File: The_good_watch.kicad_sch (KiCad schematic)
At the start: 46 parts, among them IC1 DW01A, J1 Main, J2 USB_C_Receptacle_USB2.0, J3 PROG, J4 Screen, J5 Button, J6 Conn_02x07_Counter_Clockwise, M1 Motor_DC, Q1 FS8205A, SW1 SW_Push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

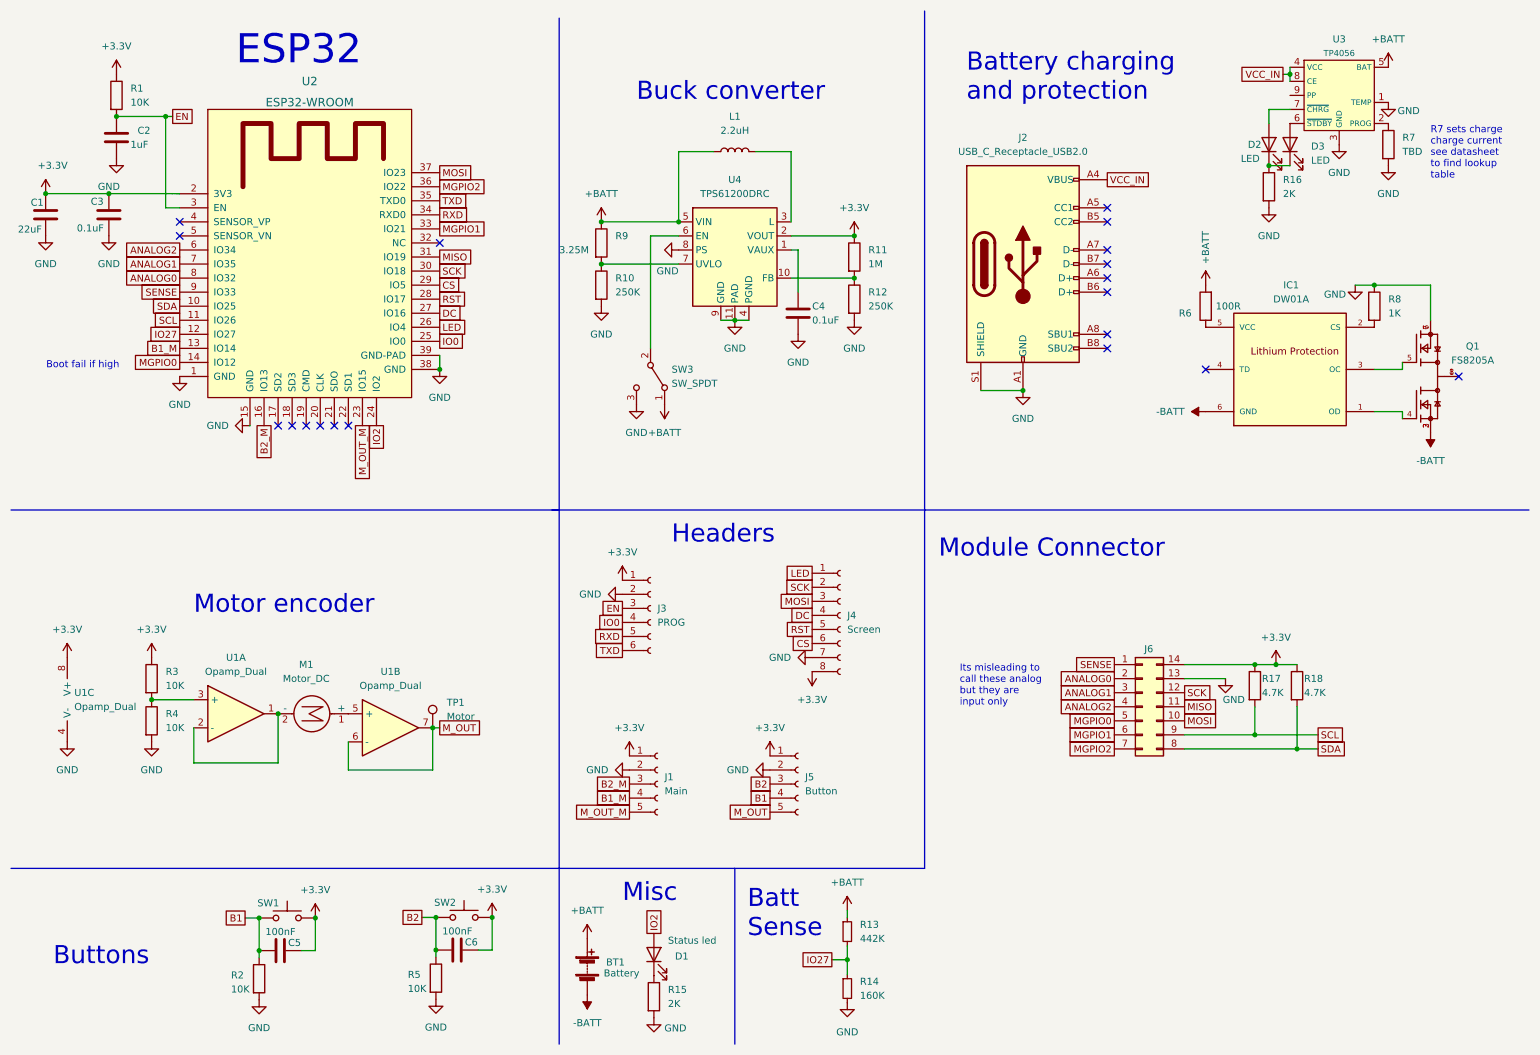
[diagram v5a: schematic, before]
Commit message: Added power switching
Uses usb power when plugged in and disconnects battery.
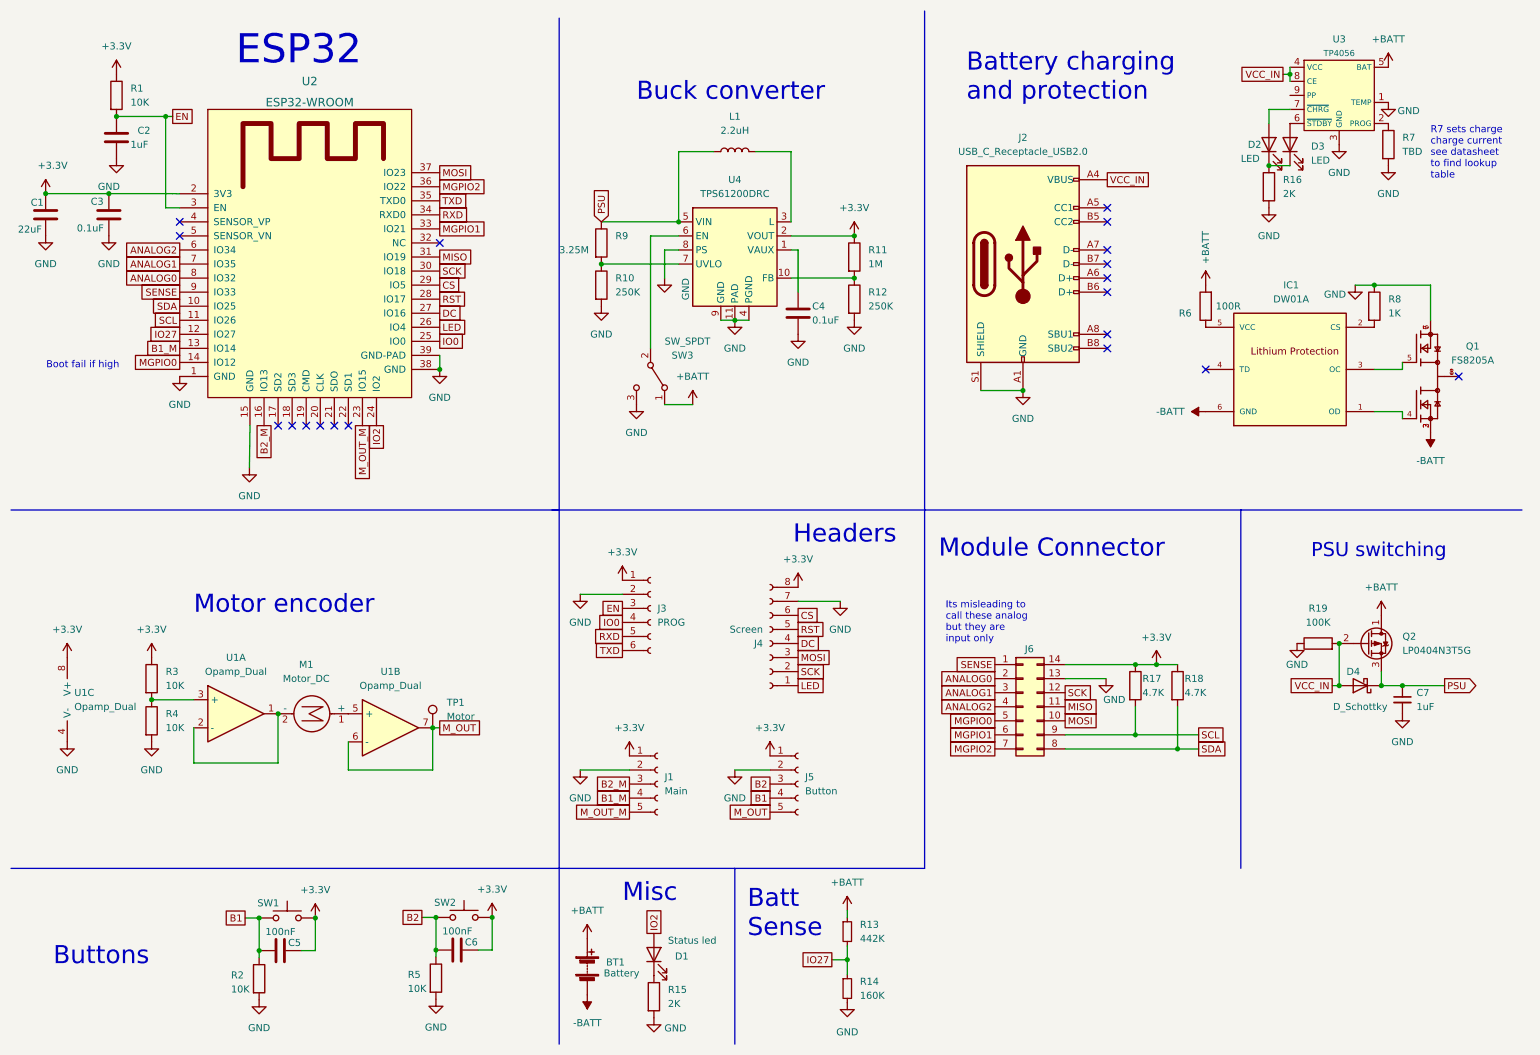
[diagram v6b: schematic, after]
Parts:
- added C7: 1uF, Capacitor_SMD:C_0805_2012Metric_Pad1.18x1.45mm_HandSolder, symbol Device:C_Small
- added D4: D_Schottky, Diode_SMD:D_0603_1608Metric, symbol Device:D_Schottky
- added Q2: LP0404N3T5G, Package_TO_SOT_SMD:SOT-883, symbol Device:Q_PMOS_DGS
- added R19: 100K, Resistor_SMD:R_0805_2012Metric, symbol Device:R
- R15, R16: footprint Resistor_SMD:R_0805_2012Metric_Pad1.20x1.40mm_HandSolder -> Resistor_SMD:R_0805_2012Metric
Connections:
- net +BATT: now also Q2.1 (D); no longer L1.1, R9.1, U4.5 (VIN)
- net GND: now also C7.2, R19.1
- net VCC_IN: now also D4.2 (A), Q2.2 (G), R19.2
- new net PSU: C7.1, D4.1 (K), L1.1, Q2.3 (S), R9.1, U4.5 (VIN)
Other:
- note added: "PSU switching"
- moved on the sheet: J4, J6, R17, R18

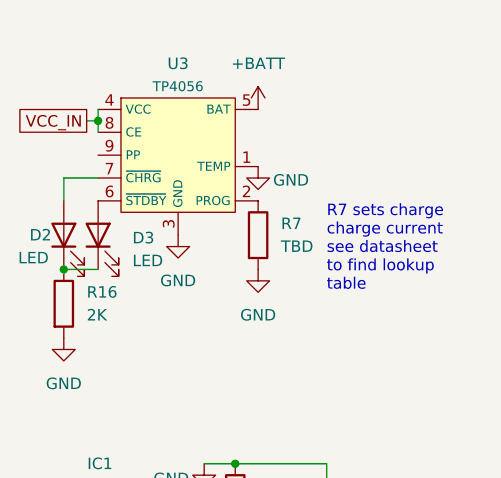
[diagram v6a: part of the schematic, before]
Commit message: Added charge current lookup table
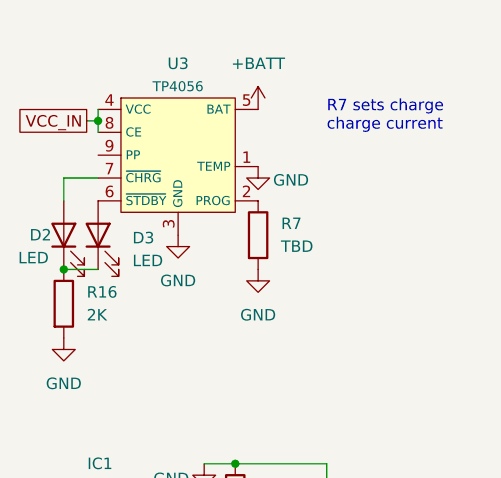
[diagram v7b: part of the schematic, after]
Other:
- note added: "R7 sets charge charge current"
- note removed: "R7 sets charge charge current see datasheet to find lookup table"

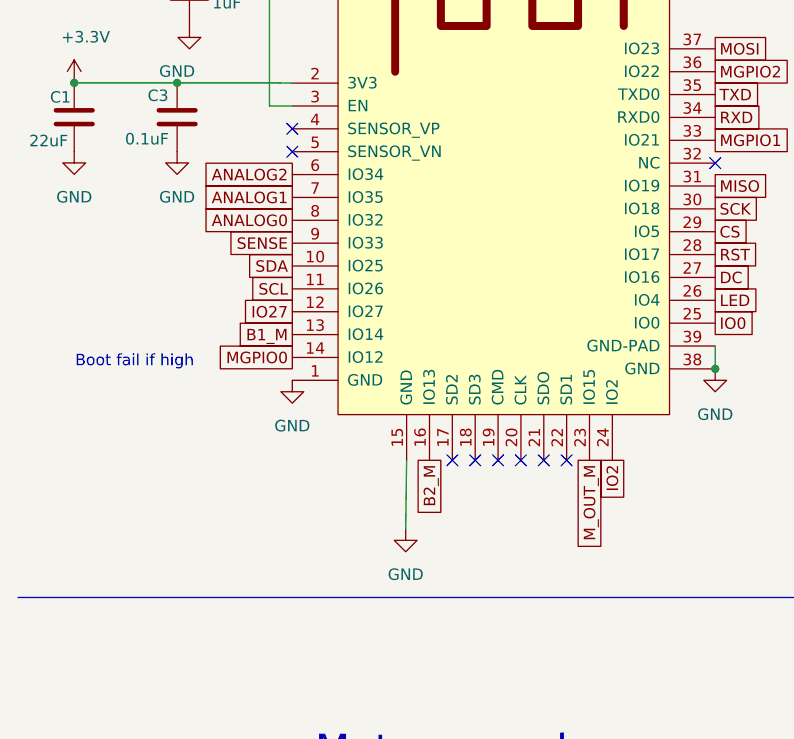
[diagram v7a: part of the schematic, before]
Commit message: Fixed analog pins
encoder pins shut down when wifi enabled now fixed
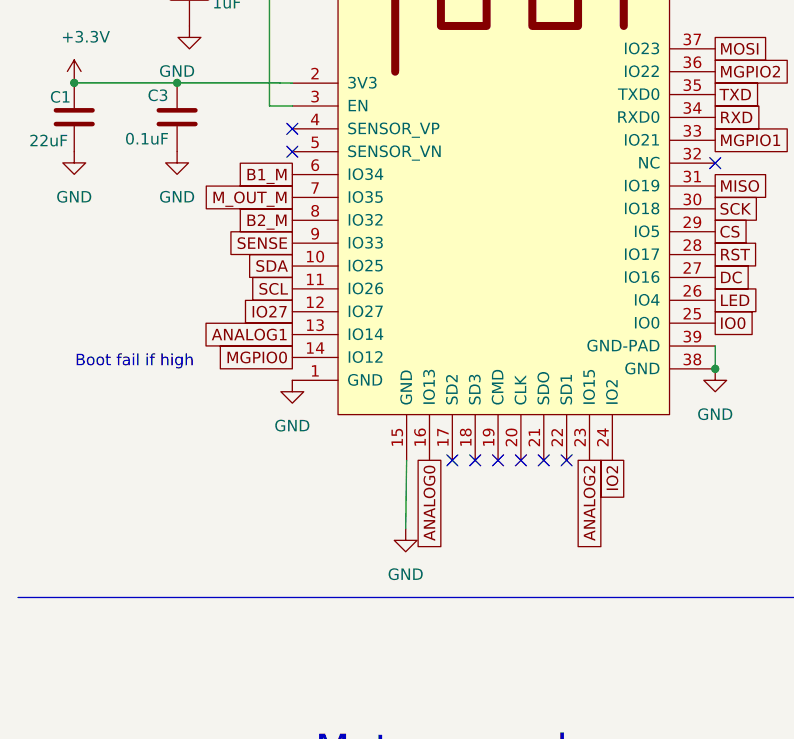
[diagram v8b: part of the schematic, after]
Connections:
- net ANALOG0: now also U2.16 (IO13); no longer U2.8 (IO32)
- net ANALOG1: now also U2.13 (IO14); no longer U2.7 (IO35)
- net ANALOG2: now also U2.23 (IO15); no longer U2.6 (IO34)
- net B1_M: now also U2.6 (IO34); no longer U2.13 (IO14)
- net B2_M: now also U2.8 (IO32); no longer U2.16 (IO13)
- net M_OUT_M: now also U2.7 (IO35); no longer U2.23 (IO15)
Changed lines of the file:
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@@
     )
   )
-  (global_label "ANALOG1" (shape passive) (at 41.91 57.15 180) (fields_autoplaced)
-    (effects (font (size 1.27 1.27)) (justify right))
-    (property "Intersheet References" "${INTERSHEET_REFS}" (id 0) (at 31.1512 57.0706 0)
-      (effects (font (size 1.27 1.27)) (justify right) hide)
-    )
-  )
-  (global_label "ANALOG2" (shape passive) (at 41.91 54.61 180) (fields_autoplaced)
-    (effects (font (size 1.27 1.27)) (justify right))
-    (property "Intersheet References" "${INTERSHEET_REFS}" (id 0) (at 31.1512 54.5306 0)
+  (global_label "ANALOG1" (shape passive) (at 41.91 72.39 180) (fields_autoplaced)
+    (effects (font (size 1.27 1.27)) (justify right))
+    (property "Intersheet References" "${INTERSHEET_REFS}" (id 0) (at 31.1512 72.3106 0)
+      (effects (font (size 1.27 1.27)) (justify right) hide)
+    )
+  )
+  (global_label "ANALOG2" (shape passive) (at 74.93 86.36 270) (fields_autoplaced)
+    (effects (font (size 1.27 1.27)) (justify right))
+    (property "Intersheet References" "${INTERSHEET_REFS}" (id 0) (at 74.8506 97.1188 90)
       (effects (font (size 1.27 1.27)) (justify right) hide)
     )
@@
     )
   )
-  (global_label "B2_M" (shape passive) (at 57.15 86.36 270) (fields_autoplaced)
-    (effects (font (size 1.27 1.27)) (justify right))
-    (property "Intersheet References" "${INTERSHEET_REFS}" (id 0) (at 57.0706 93.6717 90)
+  (global_label "B2_M" (shape passive) (at 41.91 59.69 180) (fields_autoplaced)
+    (effects (font (size 1.27 1.27)) (justify right))
+    (property "Intersheet References" "${INTERSHEET_REFS}" (id 0) (at 34.5983 59.6106 0)
       (effects (font (size 1.27 1.27)) (justify right) hide)
     )
@@
     )
   )
-  (global_label "B1_M" (shape passive) (at 41.91 72.39 180) (fields_autoplaced)
-    (effects (font (size 1.27 1.27)) (justify right))
-    (property "Intersheet References" "${INTERSHEET_REFS}" (id 0) (at 34.5983 72.3106 0)
+  (global_label "B1_M" (shape passive) (at 41.91 54.61 180) (fields_autoplaced)
+    (effects (font (size 1.27 1.27)) (justify right))
+    (property "Intersheet References" "${INTERSHEET_REFS}" (id 0) (at 34.5983 54.5306 0)
       (effects (font (size 1.27 1.27)) (justify right) hide)
     )
@@
     )
   )
-  (global_label "M_OUT_M" (shape passive) (at 74.93 86.36 270) (fields_autoplaced)
-    (effects (font (size 1.27 1.27)) (justify right))
-    (property "Intersheet References" "${INTERSHEET_REFS}" (id 0) (at 74.8506 97.2398 90)
+  (global_label "M_OUT_M" (shape passive) (at 41.91 57.15 180) (fields_autoplaced)
+    (effects (font (size 1.27 1.27)) (justify right))
+    (property "Intersheet References" "${INTERSHEET_REFS}" (id 0) (at 31.0302 57.0706 0)
       (effects (font (size 1.27 1.27)) (justify right) hide)
     )
@@
     )
   )
-  (global_label "ANALOG0" (shape passive) (at 41.91 59.69 180) (fields_autoplaced)
-    (effects (font (size 1.27 1.27)) (justify right))
-    (property "Intersheet References" "${INTERSHEET_REFS}" (id 0) (at 31.1512 59.6106 0)
-      (effects (font (size 1.27 1.27)) (justify right) hide)
-    )
+  (global_label "ANALOG0" (shape passive) (at 57.15 86.36 270) (fields_autoplaced)
+    (effects (font (size 1.27 1.27)) (justify right))
+    (property "Intersheet References" "${INTERSHEET_REFS}" (id 0) (at 57.0706 97.1188 90)
+      (effects (font (size 1.27 1.27)) (justify right) hide)
+    )
